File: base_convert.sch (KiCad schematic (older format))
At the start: 13 parts, among them J1 ISP, Q1 Q_PMOS_GSD, SW2 SELECT

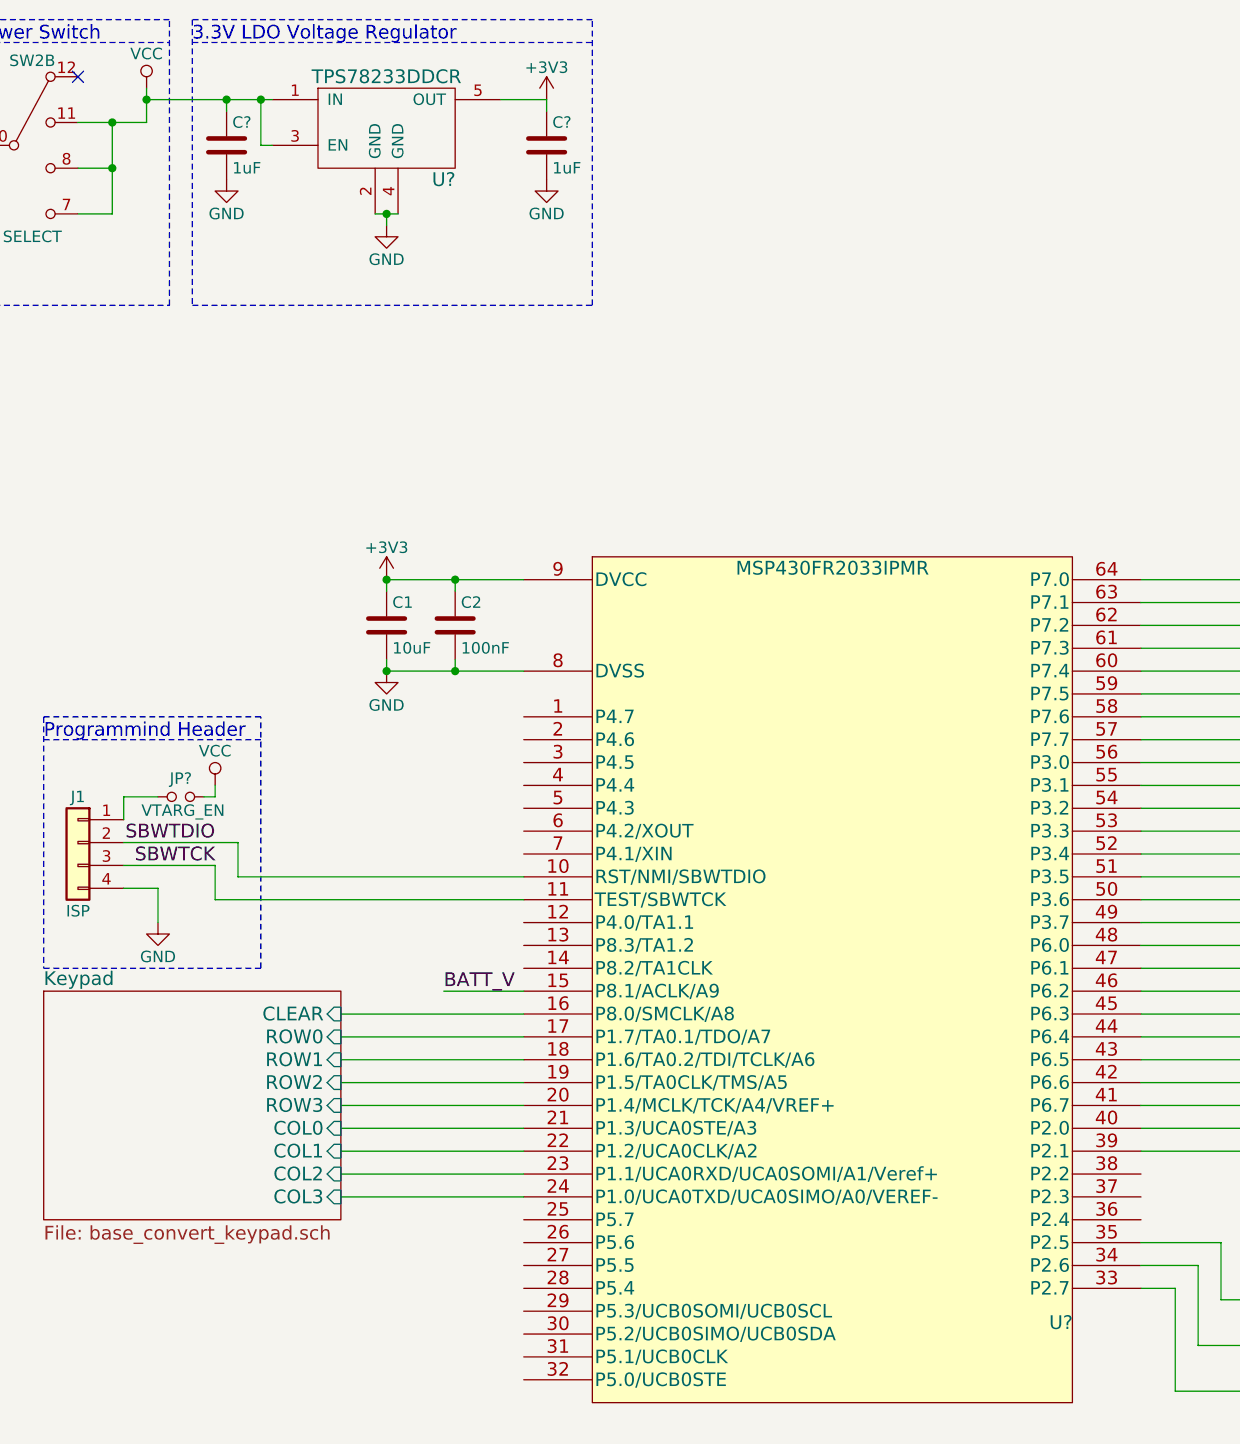
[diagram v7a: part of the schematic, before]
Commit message: anotate new components
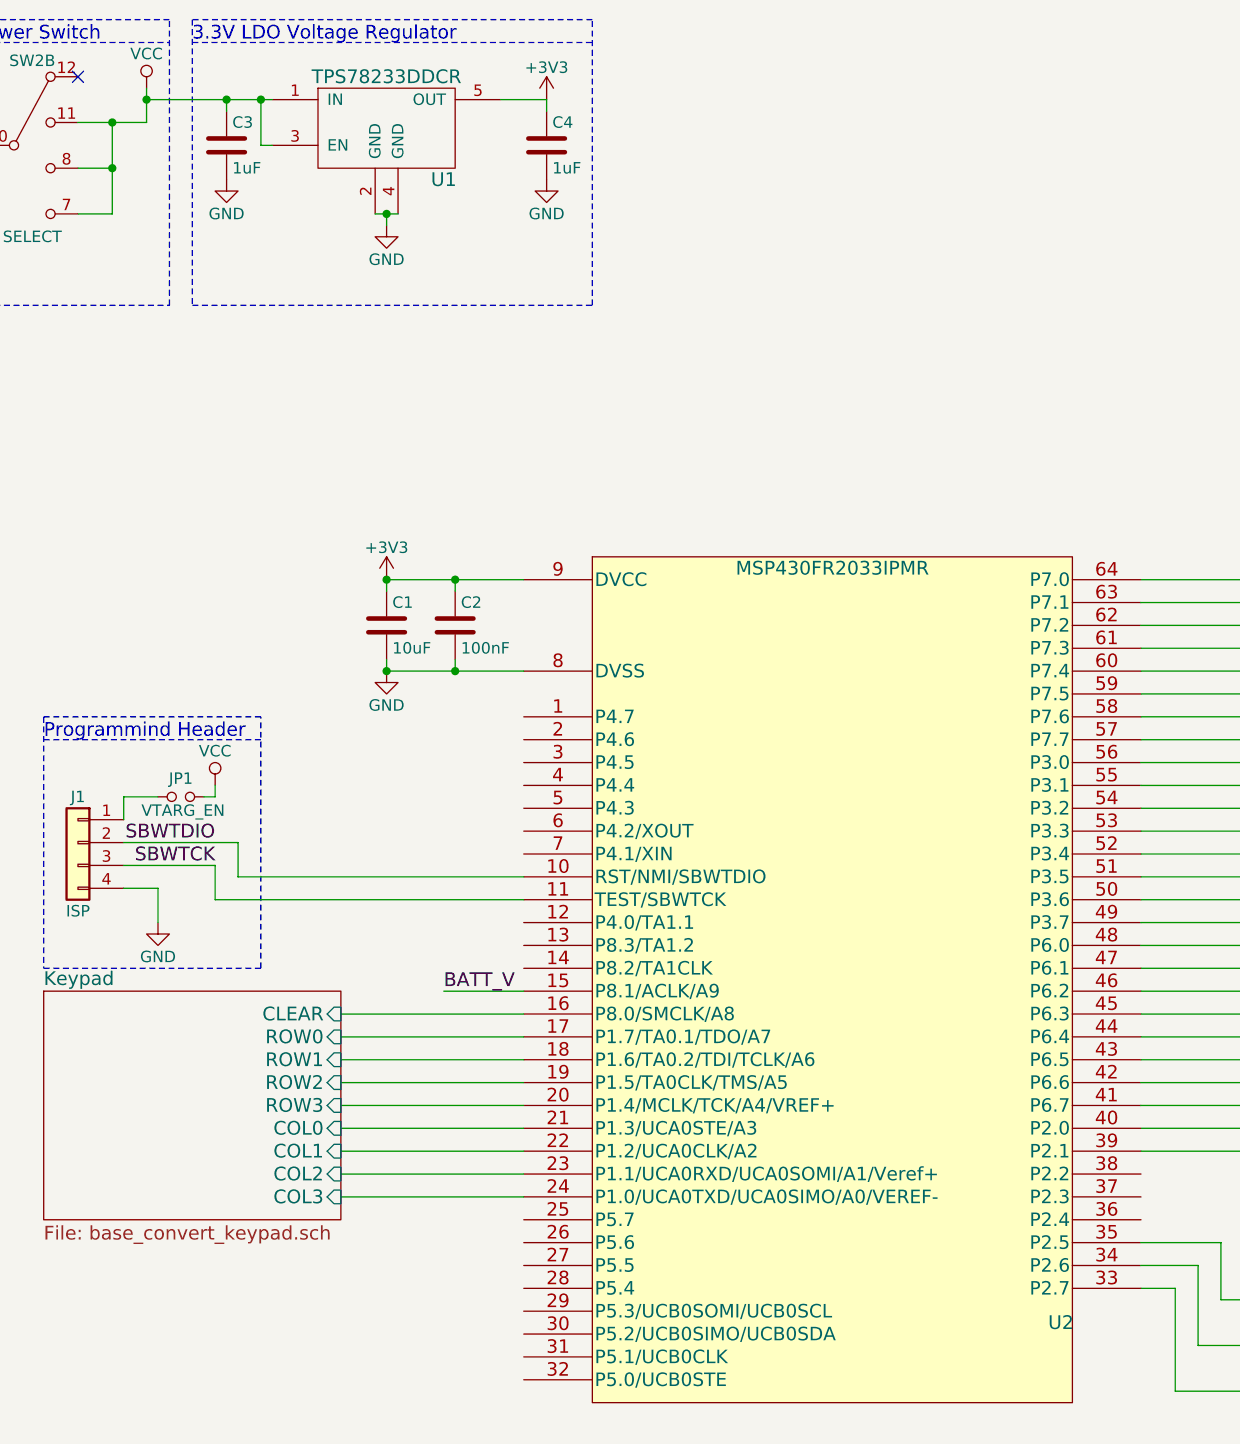
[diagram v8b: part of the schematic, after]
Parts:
- gave numbers to parts that had none: 5
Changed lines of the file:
@@
 $EndComp
 $Comp
-L GND #PWR1
+L GND #PWR3
 U 1 1 5AEC3D6F
 P 1000 1600
-F 0 "#PWR1" H 1000 1350 50  0001 C CNN
+F 0 "#PWR3" H 1000 1350 50  0001 C CNN
 F 1 "GND" H 1000 1450 50  0000 C CNN
 F 2 "" H 1000 1600 50  0001 C CNN
@@
 $EndComp
 $Comp
-L GND #PWR2
+L GND #PWR4
 U 1 1 5AEC5CE6
 P 1750 1600
-F 0 "#PWR2" H 1750 1350 50  0001 C CNN
+F 0 "#PWR4" H 1750 1350 50  0001 C CNN
 F 1 "GND" H 1750 1450 50  0000 C CNN
 F 2 "" H 1750 1600 50  0001 C CNN
@@
 $EndComp
 $Comp
-L GND #PWR5
+L GND #PWR11
 U 1 1 5AF08A85
 P 4450 3400
-F 0 "#PWR5" H 4450 3150 50  0001 C CNN
+F 0 "#PWR11" H 4450 3150 50  0001 C CNN
 F 1 "GND" H 4450 3250 50  0000 C CNN
 F 2 "" H 4450 3400 50  0001 C CNN
@@
 $EndComp
 $Comp
-L GND #PWR10
+L GND #PWR14
 U 1 1 5AF24AED
 P 10200 6500
-F 0 "#PWR10" H 10200 6250 50  0001 C CNN
+F 0 "#PWR14" H 10200 6250 50  0001 C CNN
 F 1 "GND" H 10200 6350 50  0000 C CNN
 F 2 "" H 10200 6500 50  0001 C CNN
@@
 $EndComp
 $Comp
-L GND #PWR7
+L GND #PWR2
 U 1 1 5AF3048A
 P 950 2900
-F 0 "#PWR7" H 950 2650 50  0001 C CNN
+F 0 "#PWR2" H 950 2650 50  0001 C CNN
 F 1 "GND" H 950 2750 50  0000 C CNN
 F 2 "" H 950 2900 50  0001 C CNN
@@
 $EndComp
 $Comp
-L GND #PWR9
+L GND #PWR6
 U 1 1 5AF42179
 P 3450 4500
-F 0 "#PWR9" H 3450 4250 50  0001 C CNN
+F 0 "#PWR6" H 3450 4250 50  0001 C CNN
 F 1 "GND" H 3450 4350 50  0000 C CNN
 F 2 "" H 3450 4500 50  0001 C CNN
@@
 $EndComp
 $Comp
-L VCC #PWR8
+L VCC #PWR7
 U 1 1 5AF43264
 P 3700 3900
-F 0 "#PWR8" H 3700 3750 50  0001 C CNN
+F 0 "#PWR7" H 3700 3750 50  0001 C CNN
 F 1 "VCC" H 3700 4050 50  0000 C CNN
 F 2 "" H 3700 3900 50  0001 C CNN
@@
 NoConn ~ 9550 5950
 $Comp
-L TPS782 U?
+L TPS782 U1
 U 1 1 5B28097F
 P 4450 900
-F 0 "U?" H 4700 550 60  0000 C CNN
+F 0 "U1" H 4700 550 60  0000 C CNN
 F 1 "TPS78233DDCR" H 4450 1000 60  0000 C CNN
 F 2 "" H 4450 900 60  0001 C CNN
@@
 $EndComp
 $Comp
-L C C?
+L C C3
 U 1 1 5B284652
 P 3750 1100
-F 0 "C?" H 3775 1200 50  0000 L CNN
+F 0 "C3" H 3775 1200 50  0000 L CNN
 F 1 "1uF" H 3775 1000 50  0000 L CNN
 F 2 "" H 3788 950 50  0001 C CNN
@@
 $EndComp
 $Comp
-L GND #PWR?
+L GND #PWR8
 U 1 1 5B285DA8
 P 3750 1250
-F 0 "#PWR?" H 3750 1000 50  0001 C CNN
+F 0 "#PWR8" H 3750 1000 50  0001 C CNN
 F 1 "GND" H 3750 1100 50  0000 C CNN
 F 2 "" H 3750 1250 50  0001 C CNN
@@
 $EndComp
 $Comp
-L GND #PWR?
+L GND #PWR9
 U 1 1 5B285FB6
 P 4450 1450
-F 0 "#PWR?" H 4450 1200 50  0001 C CNN
+F 0 "#PWR9" H 4450 1200 50  0001 C CNN
 F 1 "GND" H 4450 1300 50  0000 C CNN
 F 2 "" H 4450 1450 50  0001 C CNN
@@
 $EndComp
 $Comp
-L C C?
+L C C4
 U 1 1 5B2862C1
 P 5150 1100
-F 0 "C?" H 5175 1200 50  0000 L CNN
+F 0 "C4" H 5175 1200 50  0000 L CNN
 F 1 "1uF" H 5175 1000 50  0000 L CNN
 F 2 "" H 5188 950 50  0001 C CNN
@@
 $EndComp
 $Comp
-L GND #PWR?
+L GND #PWR13
 U 1 1 5B286569
 P 5150 1250
-F 0 "#PWR?" H 5150 1000 50  0001 C CNN
+F 0 "#PWR13" H 5150 1000 50  0001 C CNN
 F 1 "GND" H 5150 1100 50  0000 C CNN
 F 2 "" H 5150 1250 50  0001 C CNN
@@
 $EndComp
 $Comp
-L VCC #PWR?
+L VCC #PWR1
 U 1 1 5B28B1DA
 P 950 2150
-F 0 "#PWR?" H 950 2000 50  0001 C CNN
+F 0 "#PWR1" H 950 2000 50  0001 C CNN
 F 1 "VCC" H 950 2300 50  0000 C CNN
 F 2 "" H 950 2150 50  0001 C CNN
@@
 $EndComp
 $Comp
-L +3V3 #PWR?
+L +3V3 #PWR12
 U 1 1 5B28D631
 P 5150 900
-F 0 "#PWR?" H 5150 750 50  0001 C CNN
+F 0 "#PWR12" H 5150 750 50  0001 C CNN
 F 1 "+3V3" H 5150 1040 50  0000 C CNN
 F 2 "" H 5150 900 50  0001 C CNN
@@
 $EndComp
 $Comp
-L Jumper_NO_Small JP?
+L Jumper_NO_Small JP1
 U 1 1 5B29066B
 P 3550 3950
-F 0 "JP?" H 3550 4030 50  0000 C CNN
+F 0 "JP1" H 3550 4030 50  0000 C CNN
 F 1 "VTARG_EN" H 3560 3890 50  0000 C CNN
 F 2 "" H 3550 3950 50  0001 C CNN
@@
 Programmind Header
 $Comp
-L VCC #PWR?
+L VCC #PWR5
 U 1 1 5B29E8A8
 P 3400 850
-F 0 "#PWR?" H 3400 700 50  0001 C CNN
+F 0 "#PWR5" H 3400 700 50  0001 C CNN
 F 1 "VCC" H 3400 1000 50  0000 C CNN
 F 2 "" H 3400 850 50  0001 C CNN
@@
 3.3V LDO Voltage Regulator
 $Comp
-L +3V3 #PWR?
+L +3V3 #PWR10
 U 1 1 5B2A0C6B
 P 4450 3000
-F 0 "#PWR?" H 4450 2850 50  0001 C CNN
+F 0 "#PWR10" H 4450 2850 50  0001 C CNN
 F 1 "+3V3" H 4450 3140 50  0000 C CNN
 F 2 "" H 4450 3000 50  0001 C CNN
@@
 $EndComp
 $Comp
-L MSP430FR2033IPMR U?
+L MSP430FR2033IPMR U2
 U 1 1 5B2ADB04
 P 5050 3000
-F 0 "U?" H 7400 -250 60  0000 C CNN
+F 0 "U2" H 7400 -250 60  0000 C CNN
 F 1 "MSP430FR2033IPMR" H 6400 3050 60  0000 C CNN
 F 2 "PM64" H 6400 3150 60  0001 C CNN
